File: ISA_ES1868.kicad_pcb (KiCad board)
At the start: 4 copper layers, 104.1 x 102.9 mm, 107 parts, among them J1 LINE IN, J10 Volume buttons, J11 ISA BUS, J2 MIC, J3 Joystick/MIDI, J5 Wavetable, J7 SPKR OUT, J8 LINE OUT, U1 L78L05_TO92, U2 74LS138, U3 ES1868F, U4 93LC66, U7 LM1877, Y1 14.318Mhz

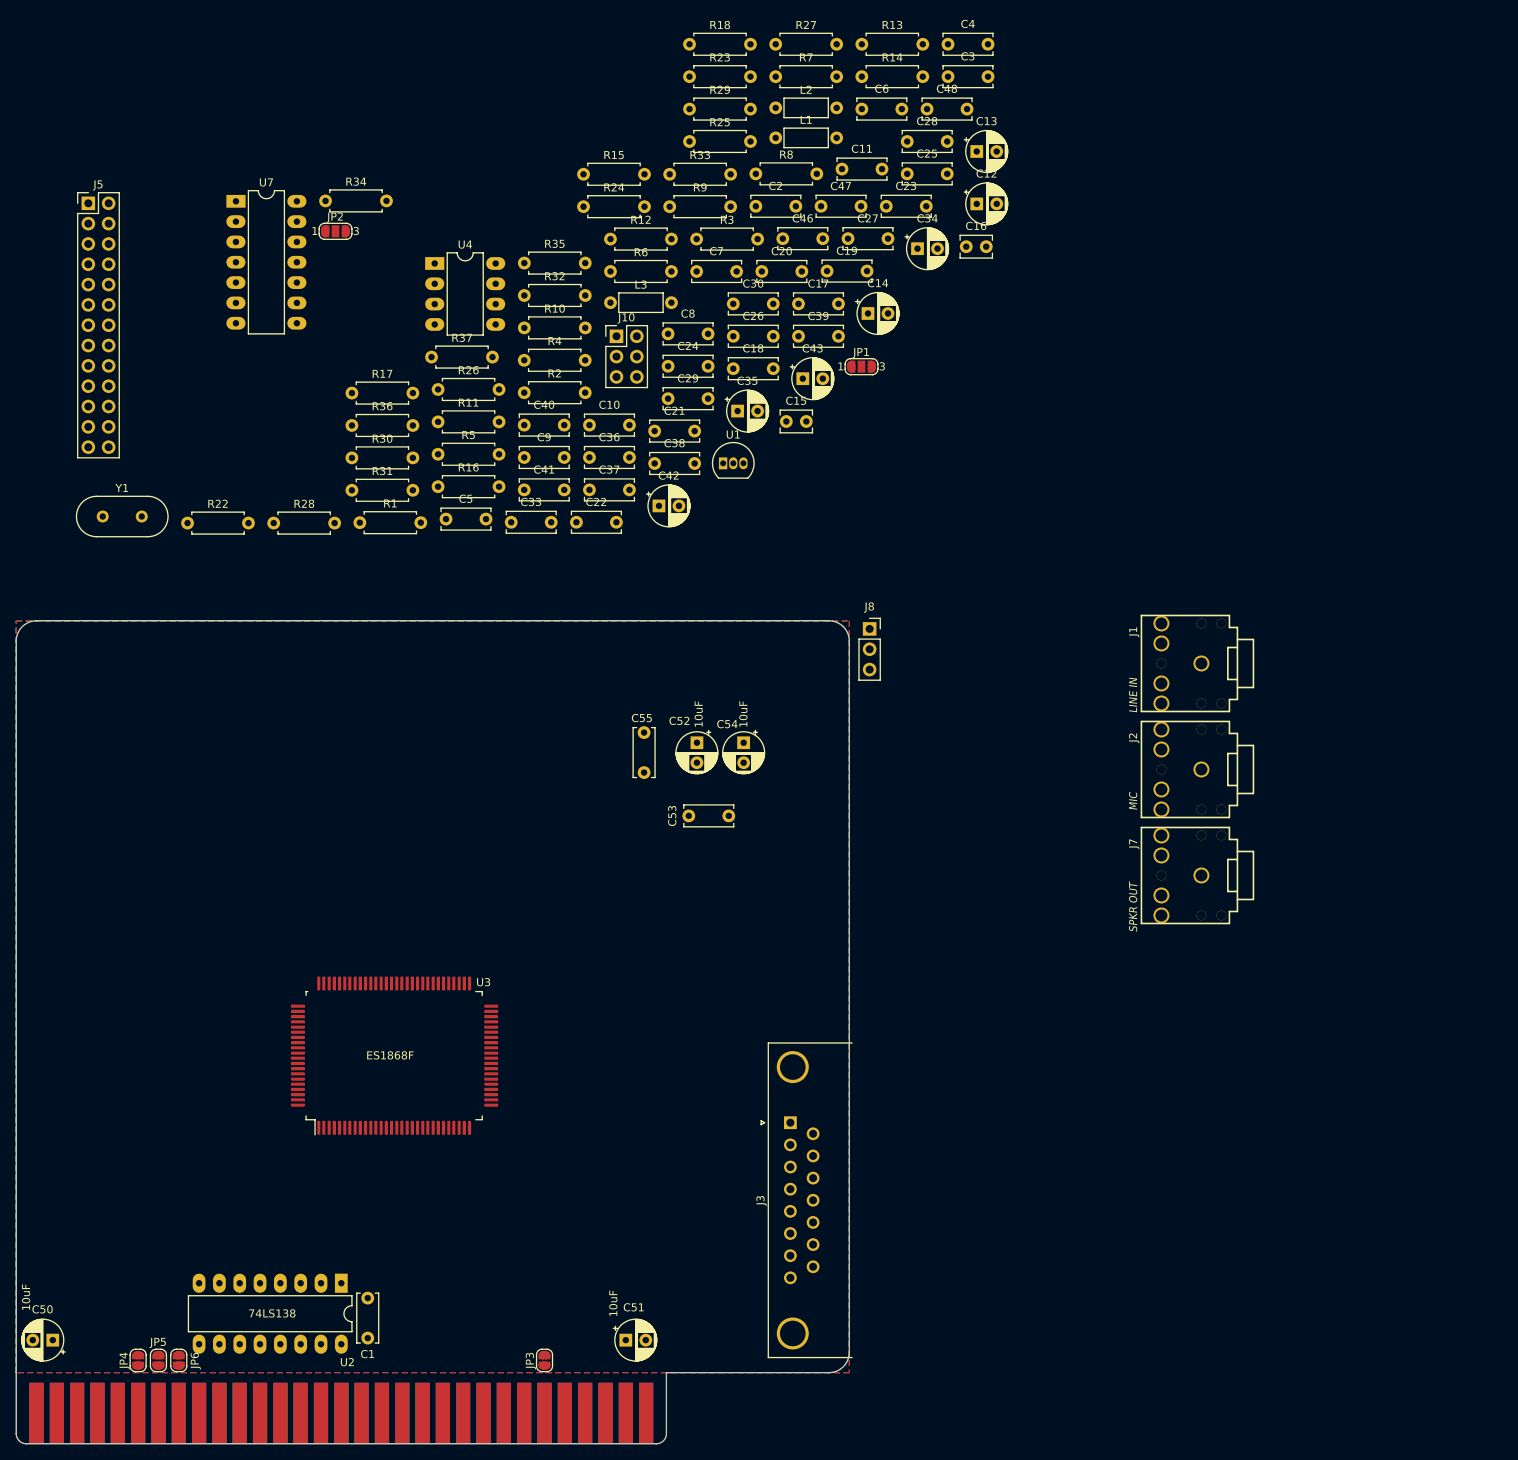
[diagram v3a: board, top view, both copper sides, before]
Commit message: start organizing things on the PCB
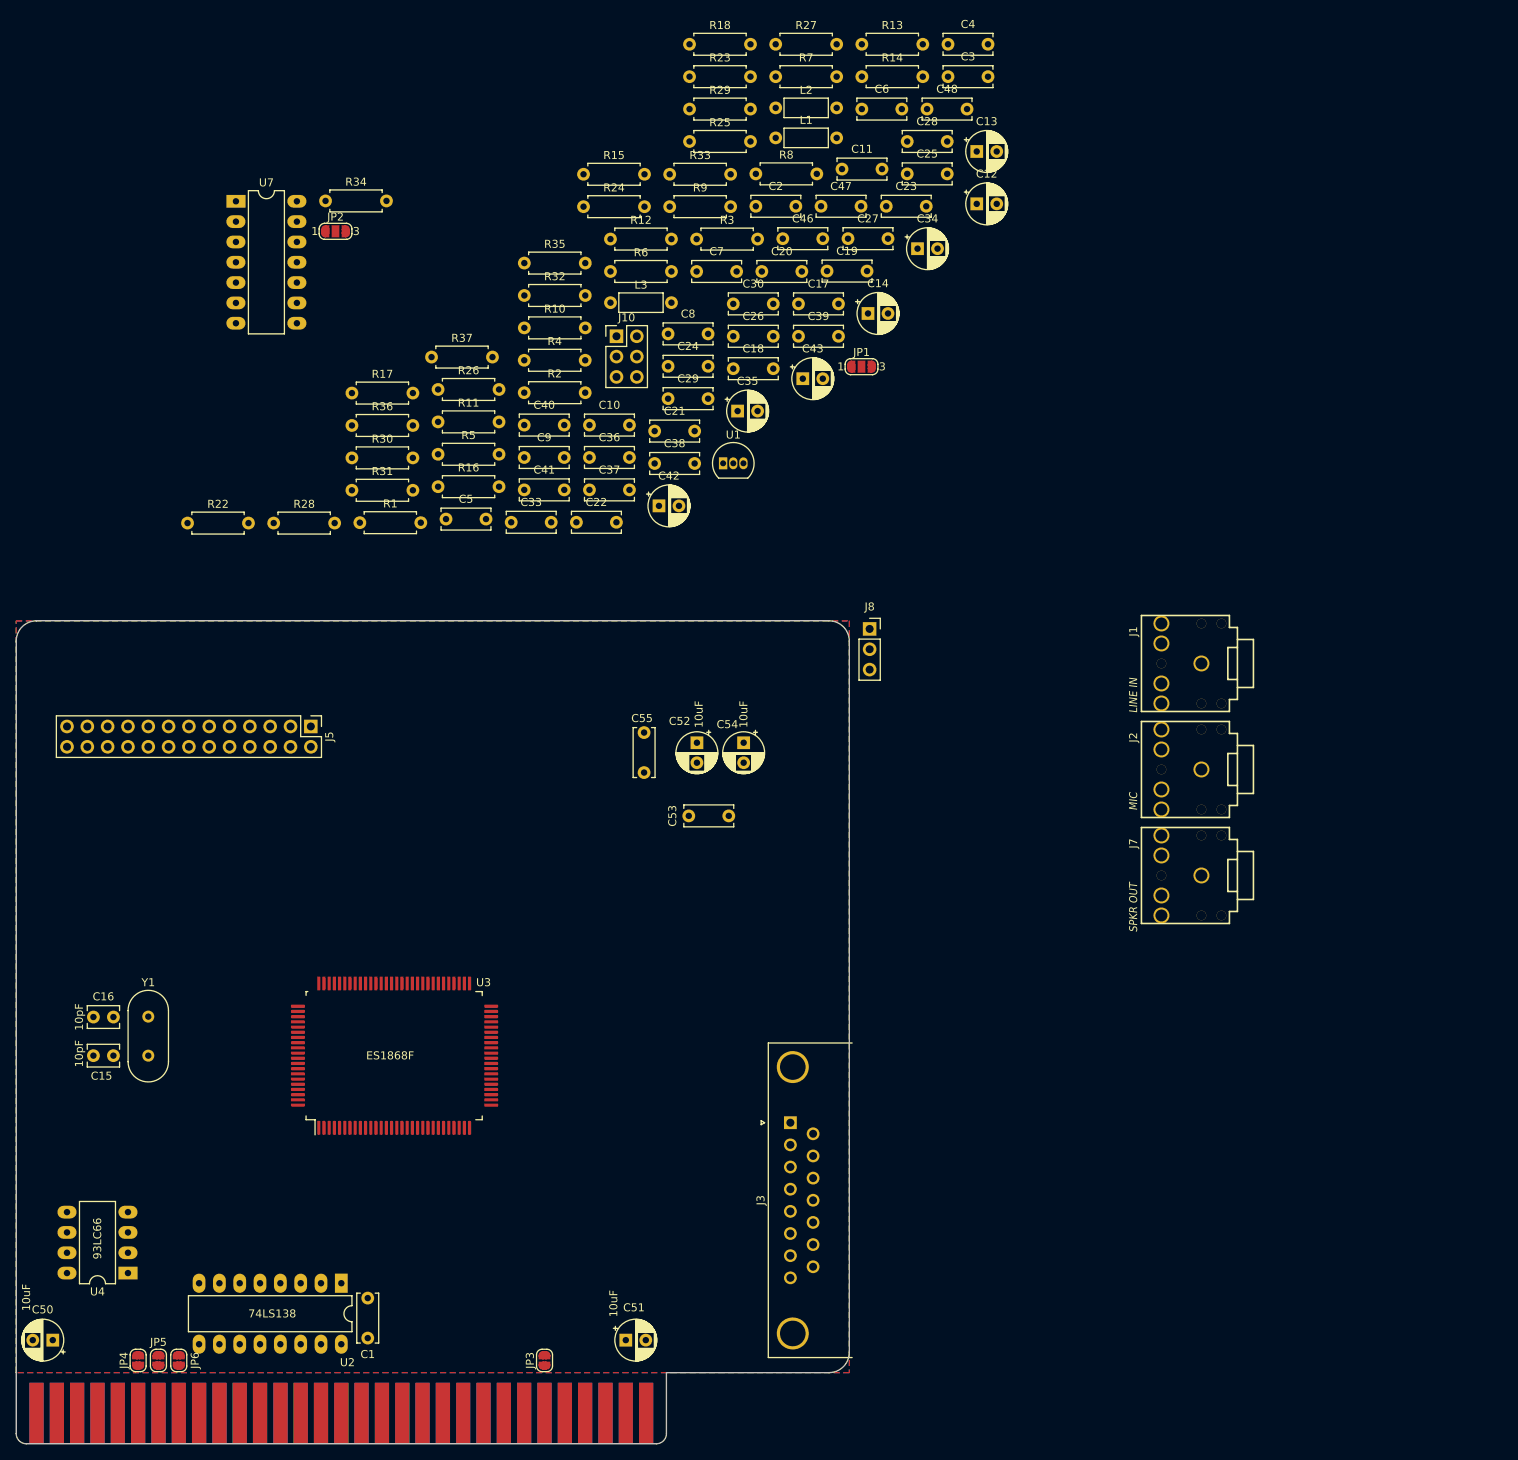
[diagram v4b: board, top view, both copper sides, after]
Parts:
- moved C16 145.5 mm to (220.5, 149.9)
- moved U4 131.9 mm to (224.8, 181.9), turned to 180 degrees
- moved C15 117.4 mm to (220.5, 154.7)
- moved J5 71.1 mm to (247.7, 113.5), turned to 270 degrees
- moved Y1 67.6 mm to (227.3, 154.7), turned to 90 degrees

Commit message: More placement on PCB
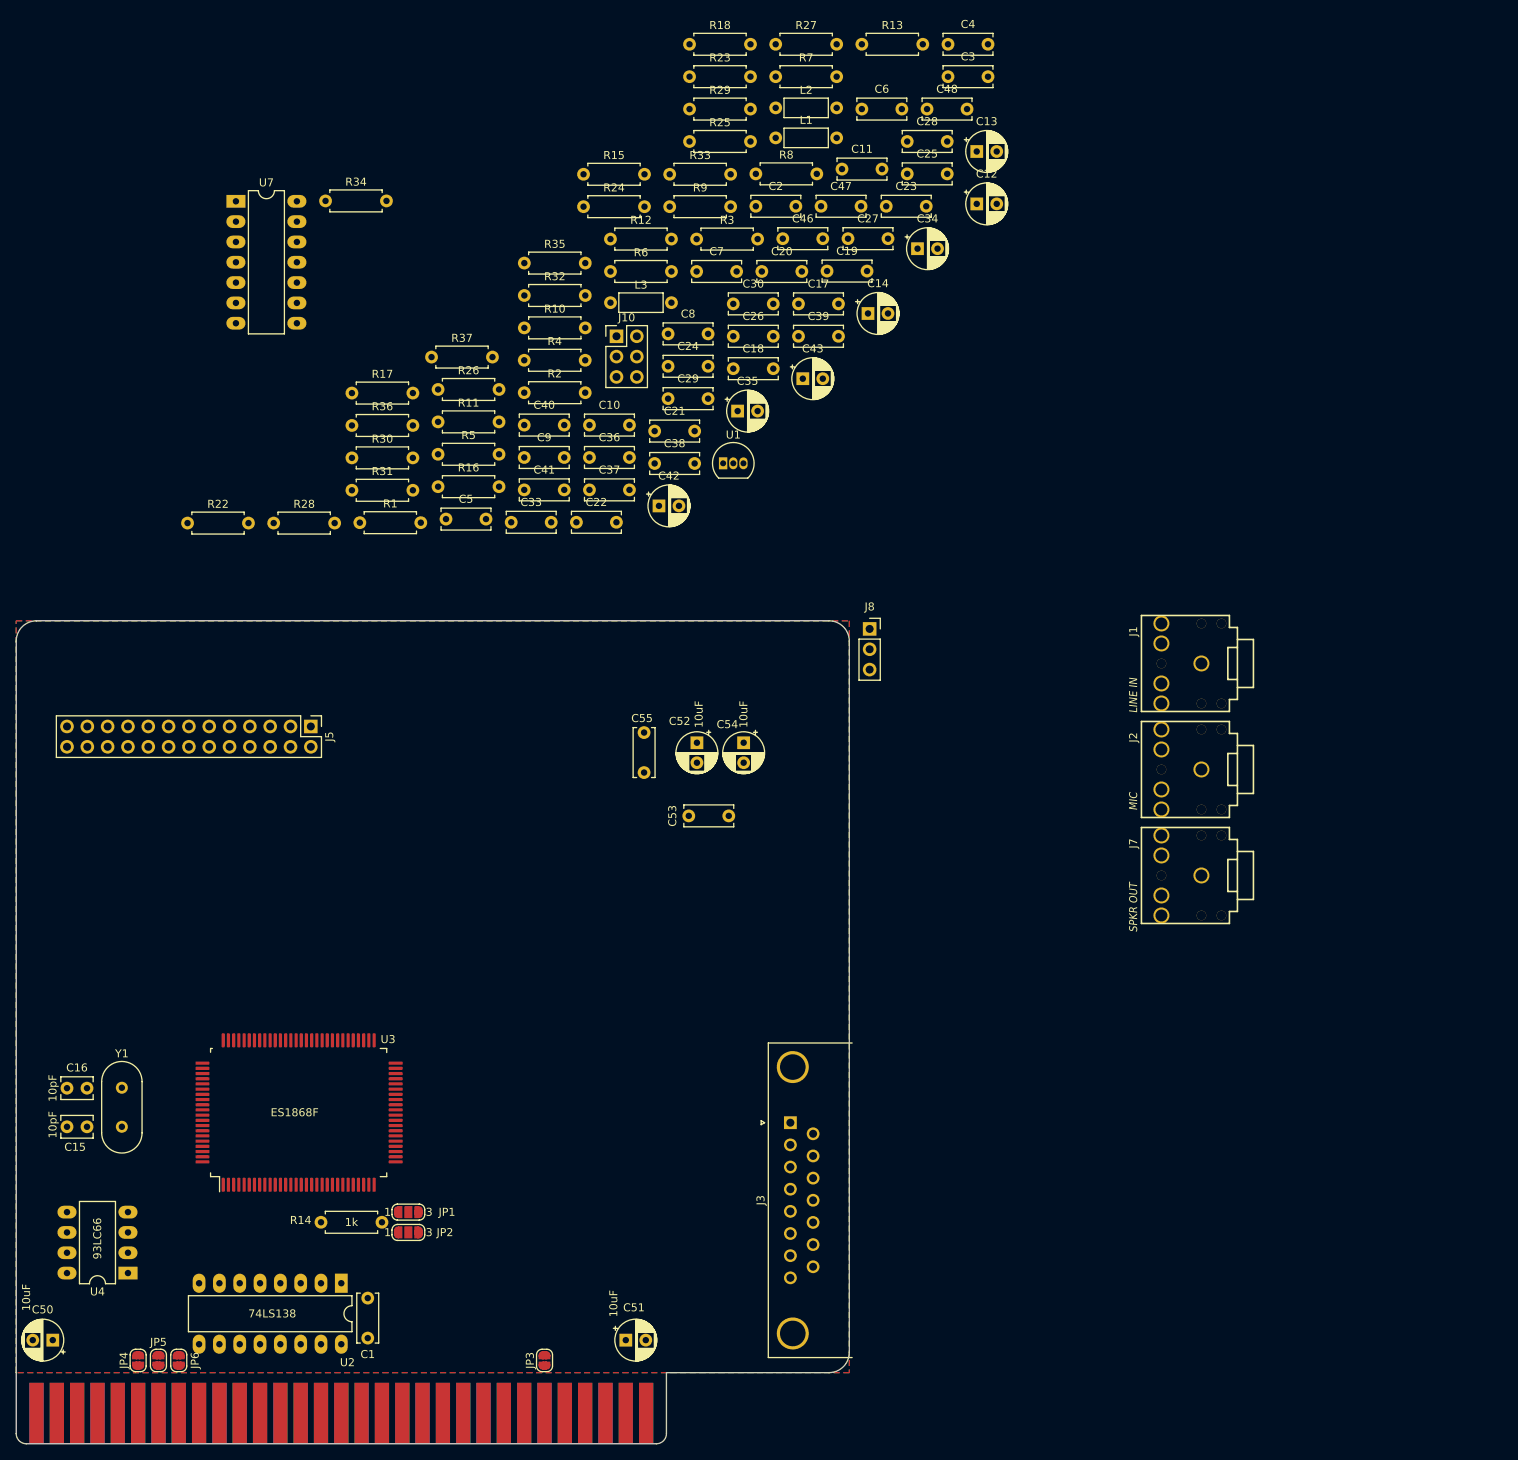
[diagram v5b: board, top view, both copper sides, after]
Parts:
- moved R14 155.3 mm to (256.5, 175.5), turned to 180 degrees
- moved JP2 125.5 mm to (259.8, 176.8)
- moved JP1 119.9 mm to (259.8, 174.2)
- moved U3 13.9 mm to (246.1, 161.8)
- moved C15 9.48 mm to (217.2, 163.6)
- moved C16 9.48 mm to (217.2, 158.8)
- moved Y1 9.48 mm to (224.0, 163.6)
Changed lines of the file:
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@@
   )
   (module Crystal:Crystal_HC49-4H_Vertical (layer F.Cu)
-    (at 227.33 154.686 90)
+    (at 224.028 163.576 90)
     (descr "Crystal THT HC-49-4H http://5hertz.com/pdfs/04404_D.pdf")
     (tags "THT crystalHC-49-4H")
@@
   )
   (module Package_QFP:LQFP-14x20mm_P0.5mm (layer F.Cu)
-    (at 258.064 154.686 90)
+    (at 246.126 161.798 90)
     (fp_text reference U3 (at 9.144 11.176) (layer F.SilkS)
       (effects (font (size 1 1) (thickness 0.15)))
@@
   )
   (module Resistor_THT:R_Axial_DIN0207_L6.3mm_D2.5mm_P7.62mm_Horizontal (layer F.Cu)
-    (at 316.526 32.314)
+    (at 256.54 175.514 180)
     (descr "Resistor, Axial_DIN0207 series, Axial, Horizontal, pin pitch=7.62mm, 0.25W = 1/4W, length*diameter=6.3*2.5mm^2, http://cdn-reichelt.de/documents/datenblatt/B400/1_4W%23YAG.pdf")
     (tags "Resistor Axial_DIN0207 series Axial Horizontal pin pitch 7.62mm 0.25W = 1/4W length 6.3mm diameter 2.5mm")
-    (fp_text reference R14 (at 3.81 -2.37) (layer F.SilkS)
+    (fp_text reference R14 (at 10.16 0.254) (layer F.SilkS)
       (effects (font (size 1 1) (thickness 0.15)))
     )
-    (fp_text value 1k (at 3.81 2.37) (layer F.Fab)
+    (fp_text value 1k (at 3.81 0) (layer F.SilkS)
       (effects (font (size 1 1) (thickness 0.15)))
     )
@@
       (effects (font (size 1 1) (thickness 0.15)))
     )
-    (pad 2 thru_hole oval (at 7.62 0) (size 1.6 1.6) (drill 0.8) (layers *.Cu *.Mask)
+    (pad 2 thru_hole oval (at 7.62 0 180) (size 1.6 1.6) (drill 0.8) (layers *.Cu *.Mask)
       (net 106 "Net-(R14-Pad2)"))
-    (pad 1 thru_hole circle (at 0 0) (size 1.6 1.6) (drill 0.8) (layers *.Cu *.Mask)
+    (pad 1 thru_hole circle (at 0 0 180) (size 1.6 1.6) (drill 0.8) (layers *.Cu *.Mask)
       (net 99 "Net-(JP2-Pad2)"))
     (model ${KISYS3DMOD}/Resistor_THT.3dshapes/R_Axial_DIN0207_L6.3mm_D2.5mm_P7.62mm_Horizontal.wrl
@@
   )
   (module Jumper:SolderJumper-3_P1.3mm_Open_RoundedPad1.0x1.5mm_NumberLabels (layer F.Cu)
-    (at 250.736 51.644)
+    (at 259.842 176.784)
     (descr "SMD Solder 3-pad Jumper, 1x1.5mm rounded Pads, 0.3mm gap, open, labeled with numbers")
     (tags "solder jumper open")
     (attr virtual)
-    (fp_text reference JP2 (at 0 -1.8) (layer F.SilkS)
+    (fp_text reference JP2 (at 4.572 0) (layer F.SilkS)
       (effects (font (size 1 1) (thickness 0.15)))
     )
@@
   )
   (module Jumper:SolderJumper-3_P1.3mm_Open_RoundedPad1.0x1.5mm_NumberLabels (layer F.Cu)
-    (at 316.486 68.564)
+    (at 259.842 174.244)
     (descr "SMD Solder 3-pad Jumper, 1x1.5mm rounded Pads, 0.3mm gap, open, labeled with numbers")
     (tags "solder jumper open")
     (attr virtual)
-    (fp_text reference JP1 (at 0 -1.8) (layer F.SilkS)
+    (fp_text reference JP1 (at 4.826 0) (layer F.SilkS)
       (effects (font (size 1 1) (thickness 0.15)))
     )
@@
   )
   (module Capacitor_THT:C_Disc_D3.8mm_W2.6mm_P2.50mm (layer F.Cu)
-    (at 220.472 149.86)
+    (at 217.17 158.75)
     (descr "C, Disc series, Radial, pin pitch=2.50mm, , diameter*width=3.8*2.6mm^2, Capacitor, http://www.vishay.com/docs/45233/krseries.pdf")
     (tags "C Disc series Radial pin pitch 2.50mm  diameter 3.8mm width 2.6mm Capacitor")
@@
   )
   (module Capacitor_THT:C_Disc_D3.8mm_W2.6mm_P2.50mm (layer F.Cu)
-    (at 220.472 154.686)
+    (at 217.17 163.576)
     (descr "C, Disc series, Radial, pin pitch=2.50mm, , diameter*width=3.8*2.6mm^2, Capacitor, http://www.vishay.com/docs/45233/krseries.pdf")
     (tags "C Disc series Radial pin pitch 2.50mm  diameter 3.8mm width 2.6mm Capacitor")
